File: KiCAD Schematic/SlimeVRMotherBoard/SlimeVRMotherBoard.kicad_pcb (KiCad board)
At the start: 2 copper layers, 54 x 54 mm, 14 parts, among them U1 4056Board, U2 WeMos_D1_mini, U3 BN008X, U4 BN008X

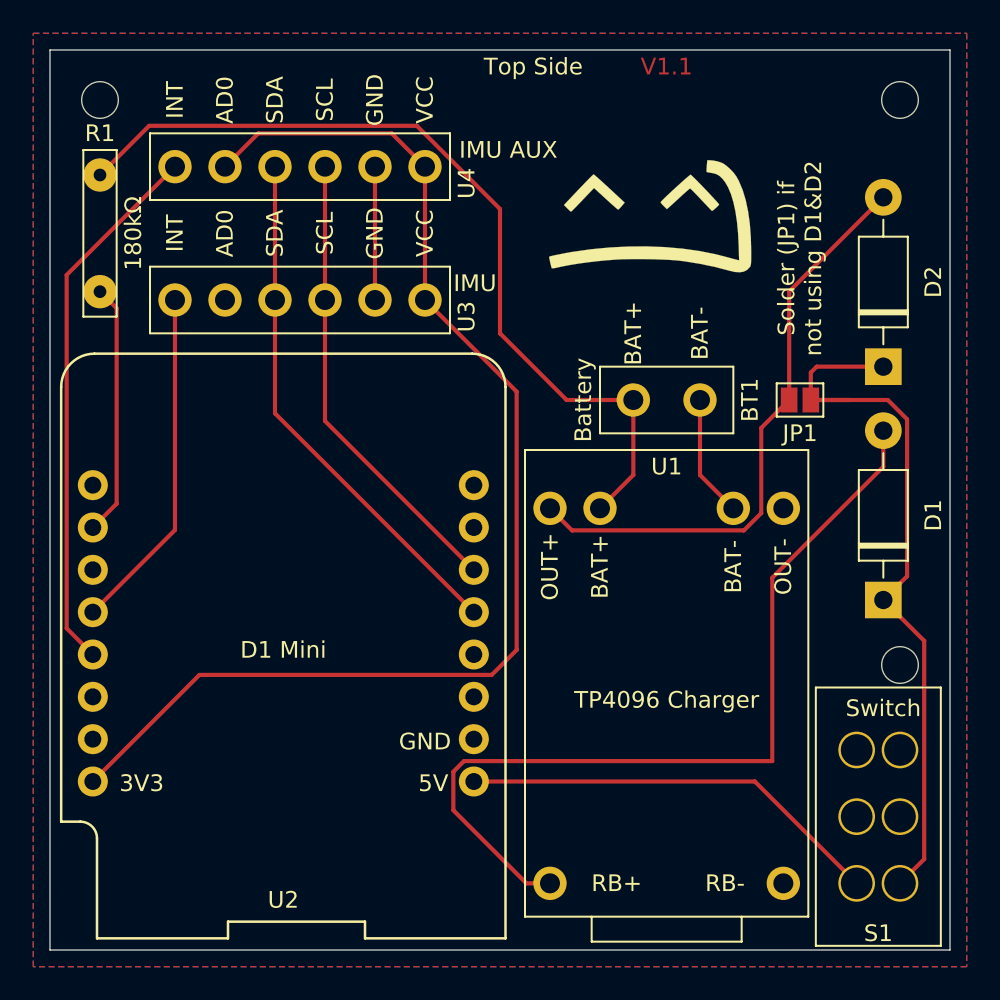
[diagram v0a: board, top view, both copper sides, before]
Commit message: Updated board to V1.2 that fixed switch issue. Added new stl's for IMU cases
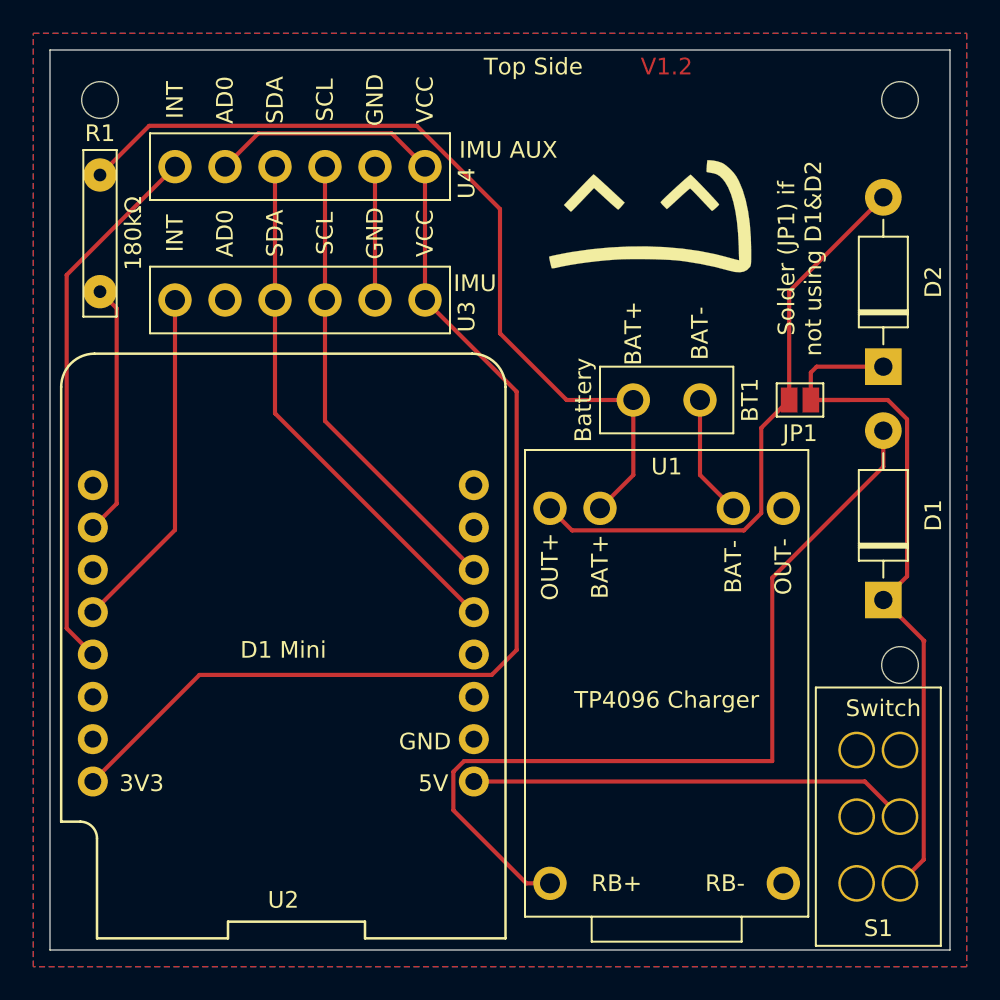
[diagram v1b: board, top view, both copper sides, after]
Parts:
- moved G*** 0.81 mm to (167.2, 103.6)
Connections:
- U1 pad 6: Net-(U1-Pad6) -> unconnected-(U1-Pad6)
- U2 pad 1: Net-(U2-Pad1) -> unconnected-(U2-Pad1)
- U2 pad 11: Net-(U2-Pad11) -> unconnected-(U2-Pad11)
- U2 pad 12: Net-(U2-Pad12) -> unconnected-(U2-Pad12)
- U2 pad 15: Net-(U2-Pad15) -> unconnected-(U2-Pad15)
- U2 pad 16: Net-(U2-Pad16) -> unconnected-(U2-Pad16)
- U2 pad 3: Net-(U2-Pad3) -> unconnected-(U2-Pad3)
- U2 pad 6: Net-(U2-Pad6) -> unconnected-(U2-Pad6)
- U2 pad 7: Net-(U2-Pad7) -> unconnected-(U2-Pad7)
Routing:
- net Net-(S1-Pad2): track 25.5 -> 26.4 mm
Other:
- net class Default removed
- board text added: "V1.2"
- board text removed: "V1.1"
